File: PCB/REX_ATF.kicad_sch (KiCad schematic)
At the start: 9 parts, among them J1 Tandy_100_102_200_option_rom, J2 JTAG, U1 ATF1504ASL-xAx44, U2 29F800BB

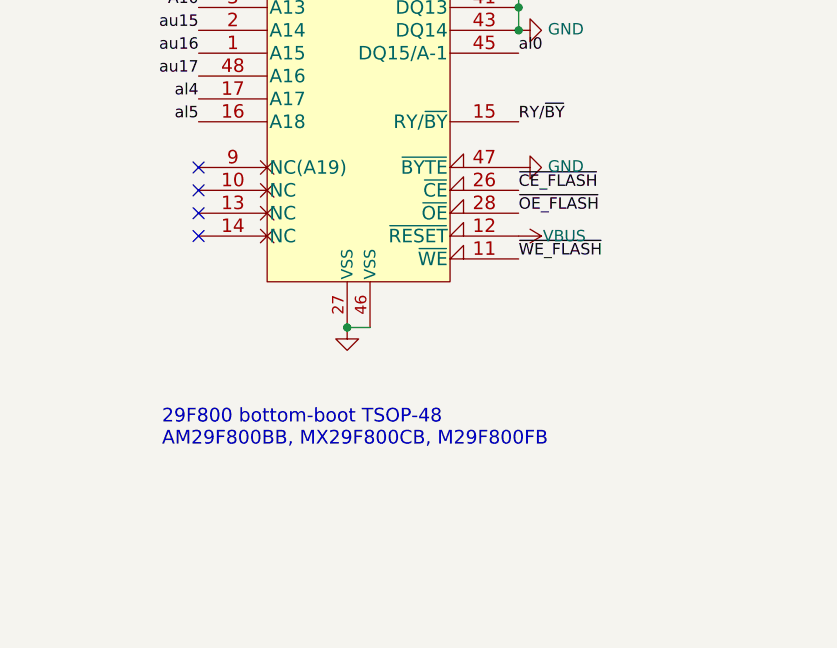
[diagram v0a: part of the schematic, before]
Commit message: use nc pins for pcb ground path
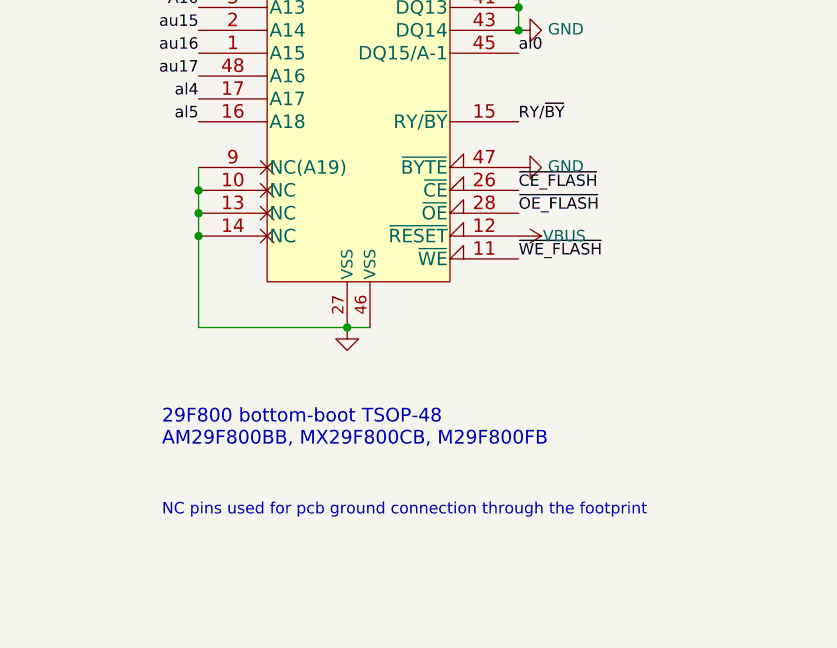
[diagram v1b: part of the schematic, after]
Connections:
- net GND: now also U2.10 (NC), U2.13 (NC), U2.14 (NC), U2.9 (NC(A19))
- no-connect marks 13 -> 9
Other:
- note added: "NC pins used for pcb ground connection through the footprint"
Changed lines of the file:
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@@
 	(title_block
 		(title "REX ATF")
-		(date "2024-07-08")
-		(rev "001")
+		(date "2024-07-22")
+		(rev "002")
 		(company "Brian K. White - b.kenyon.w@gmail.com")
 		(comment 1 "Original design: Steven Adolph")
@@
 	)
 	(junction
+		(at 210.82 104.14)
+		(diameter 0)
+		(color 0 0 0 0)
+	)
+	(junction
 		(at 148.59 113.03)
 		(diameter 0)
@@
 	)
 	(junction
+		(at 210.82 109.22)
+		(diameter 0)
+		(color 0 0 0 0)
+	)
+	(junction
+		(at 210.82 106.68)
+		(diameter 0)
+		(color 0 0 0 0)
+	)
+	(junction
 		(at 146.05 113.03)
 		(diameter 0)
@@
 	)
 	(no_connect
-		(at 210.82 104.14)
-	)
-	(no_connect
-		(at 210.82 109.22)
-	)
-	(no_connect
 		(at 127 69.85)
 	)
@@
 		(at 54.61 67.31)
 	)
-	(no_connect
-		(at 210.82 106.68)
-	)
-	(no_connect
-		(at 210.82 101.6)
-	)
 	(wire
 		(pts
@@
 	(wire
 		(pts
+			(xy 210.82 101.6) (xy 210.82 104.14)
+		)
+		(stroke
+			(width 0)
+			(type default)
+		)
+	)
+	(wire
+		(pts
+			(xy 210.82 109.22) (xy 210.82 119.38)
+		)
+		(stroke
+			(width 0)
+			(type default)
+		)
+	)
+	(wire
+		(pts
 			(xy 246.38 71.12) (xy 246.38 73.66)
 		)
@@
 	(wire
 		(pts
+			(xy 210.82 106.68) (xy 210.82 109.22)
+		)
+		(stroke
+			(width 0)
+			(type default)
+		)
+	)
+	(wire
+		(pts
 			(xy 246.38 73.66) (xy 246.38 76.2)
 		)
@@
 	(wire
 		(pts
+			(xy 210.82 119.38) (xy 227.33 119.38)
+		)
+		(stroke
+			(width 0)
+			(type default)
+		)
+	)
+	(wire
+		(pts
 			(xy 143.51 41.91) (xy 146.05 41.91)
 		)
@@
 	(wire
 		(pts
+			(xy 210.82 104.14) (xy 210.82 106.68)
+		)
+		(stroke
+			(width 0)
+			(type default)
+		)
+	)
+	(wire
+		(pts
 			(xy 148.59 41.91) (xy 151.13 41.91)
 		)
@@
 		)
 	)
+	(text "NC pins used for pcb ground connection through the footprint"
+		(exclude_from_sim no)
+		(at 206.756 139.7 0)
+		(effects
+			(font
+				(size 1.27 1.27)
+			)
+			(justify left)
+		)
+	)

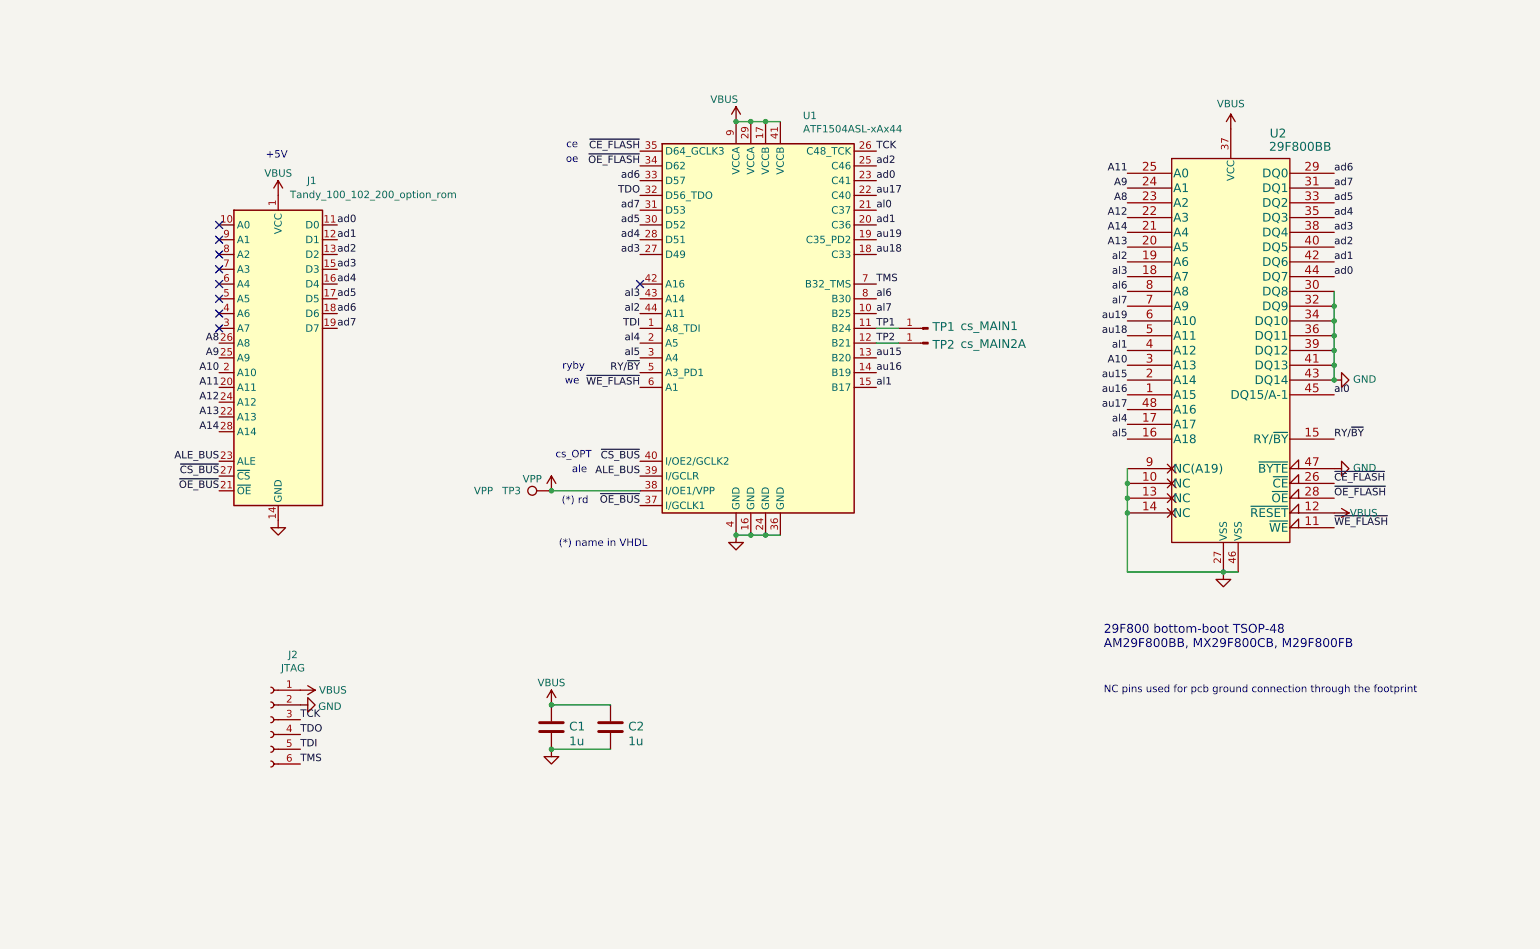
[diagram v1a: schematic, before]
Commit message: move ALE to a GCLK pin and init /CSA & /CSB high
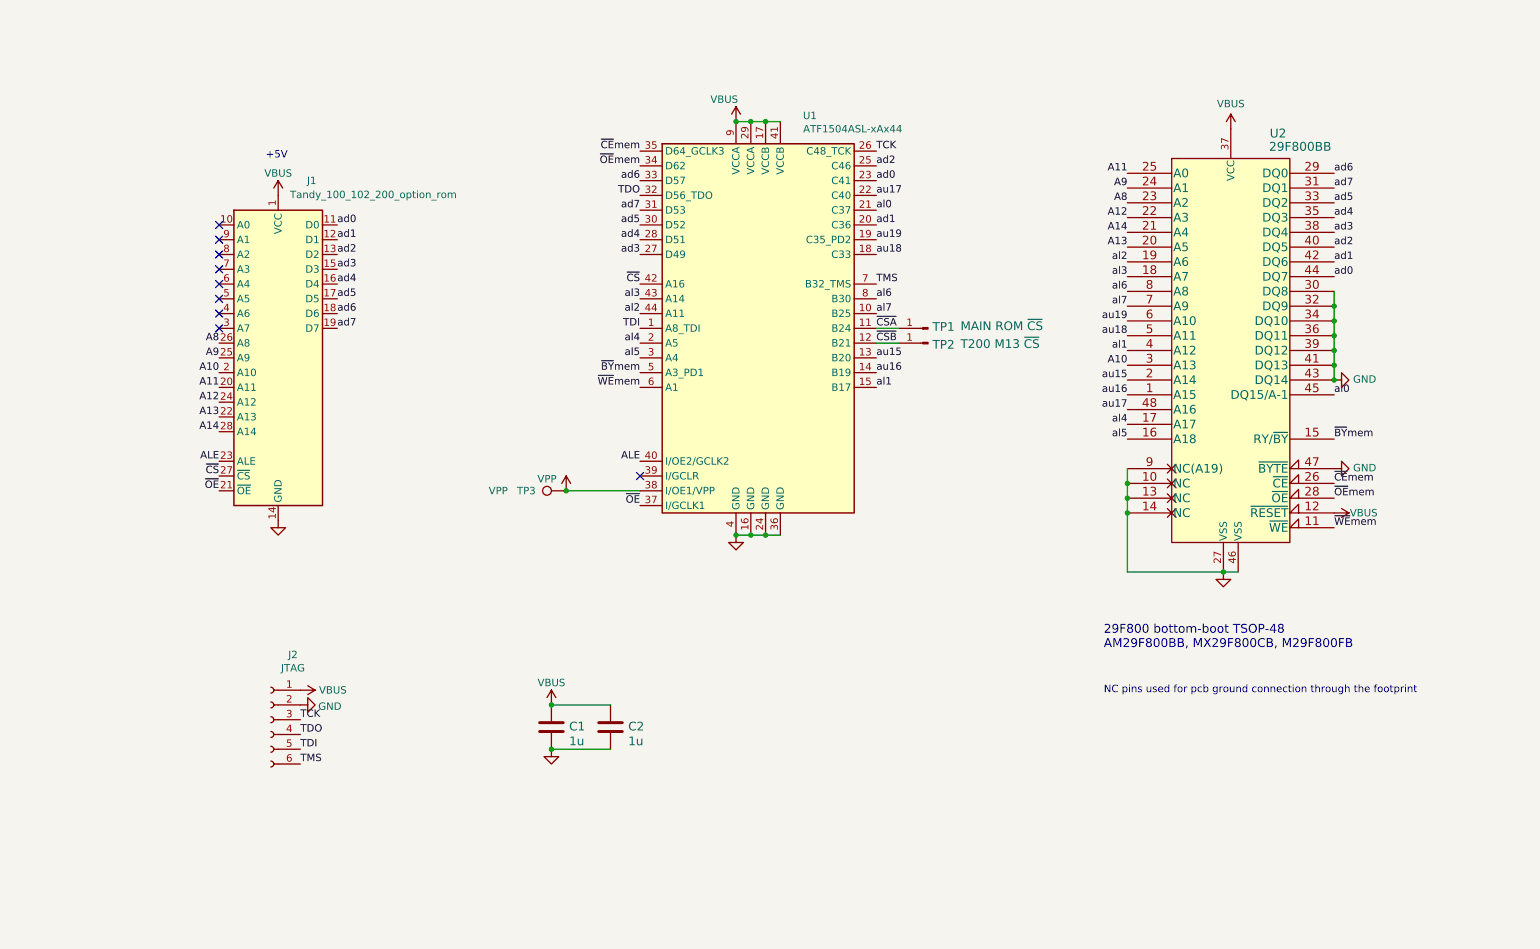
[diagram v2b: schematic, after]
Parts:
- TP1: value cs_MAIN1 -> MAIN ROM ~{CS}
- TP2: value cs_MAIN2A -> T200 M13 ~{CS}
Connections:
- net ~{CS}: now reaches U1.42 (A16)
- net ~{CS}: now also J1.27 (~{CS})
- net ALE_BUS: no longer names the net of U1.39 (I/GCLR)
- net ALE_BUS: no longer J1.23 (ALE)
- net RY/~{BY} renamed ~{BY}mem
- net TP1 renamed ~{CSA}
- net TP2 renamed ~{CSB}
- net ~{CE_FLASH} renamed ~{CE}mem
- net ~{CS_BUS} renamed ALE
- net ALE: now also J1.23 (ALE); no longer J1.27 (~{CS})
- net ~{OE_BUS} renamed ~{OE}
- net ~{OE_FLASH} renamed ~{OE}mem
- net ~{WE_FLASH} renamed ~{WE}mem
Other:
- note removed: "(*) name in VHDL"
- note removed: "(*) rd"
- note removed: "ale"
- note removed: "ce"
- note removed: "cs_OPT"
- note removed: "oe"
- note removed: "ryby"
- note removed: "we"
- moved on the sheet: TP3
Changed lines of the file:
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@@
 	(title_block
 		(title "REX ATF")
-		(date "2024-07-22")
-		(rev "002")
+		(date "2024-07-23")
+		(rev "004")
 		(company "Brian K. White - b.kenyon.w@gmail.com")
 		(comment 1 "Original design: Steven Adolph")
@@
 	)
 	(junction
-		(at 111.76 105.41)
+		(at 114.3 105.41)
 		(diameter 0)
 		(color 0 0 0 0)
@@
 	)
 	(no_connect
-		(at 127 69.85)
+		(at 127 102.87)
 	)
 	(no_connect
@@
 	(wire
 		(pts
-			(xy 111.76 105.41) (xy 127 105.41)
+			(xy 114.3 105.41) (xy 127 105.41)
 		)
 		(stroke
@@
 		)
 	)
-	(text "(*) rd"
-		(exclude_from_sim no)
-		(at 115.824 107.188 0)
-		(effects
-			(font
-				(size 1.27 1.27)
-			)
-		)
-	)
-	(text "ryby"
-		(exclude_from_sim no)
-		(at 115.57 84.074 0)
-		(effects
-			(font
-				(size 1.27 1.27)
-			)
-		)
-	)
-	(text "oe"
-		(exclude_from_sim no)
-		(at 115.316 48.514 0)
-		(effects
-			(font
-				(size 1.27 1.27)
-			)
-		)
-	)
 	(text "29F800 bottom-boot TSOP-48\nAM29F800BB, MX29F800CB, M29F800FB"
 		(exclude_from_sim no)
@@
 		)
 	)
-	(text "ale"
-		(exclude_from_sim no)
-		(at 116.586 101.854 0)
-		(effects
-			(font
-				(size 1.27 1.27)
-			)
-		)
-	)
-	(text "we"
-		(exclude_from_sim no)
-		(at 115.316 86.614 0)
-		(effects
-			(font
-				(size 1.27 1.27)
-			)
-		)
-	)
 	(text "NC pins used for pcb ground connection through the footprint"
 		(exclude_from_sim no)
@@
 		)
 	)
-	(text "(*) name in VHDL"
-		(exclude_from_sim no)
-		(at 113.03 114.554 0)
-		(effects
-			(font
-				(size 1.27 1.27)
-			)
-			(justify left)
-		)
-	)
-	(text "cs_OPT"
-		(exclude_from_sim no)
-		(at 115.57 99.314 0)
-		(effects
-			(font
-				(size 1.27 1.27)
-			)
-		)
-	)
-	(text "ce"
-		(exclude_from_sim no)
-		(at 115.316 45.974 0)
-		(effects
-			(font
-				(size 1.27 1.27)
-			)
-		)
-	)
 	(label "au17"
 		(at 210.82 91.44 180)
@@
 		)
 	)
-	(label "ALE_BUS"
-		(at 127 102.87 180)
-		(fields_autoplaced yes)
-		(effects
-			(font
-				(size 1.27 1.27)
-			)
-			(justify right bottom)
-		)
-	)
-	(label "ALE_BUS"
+	(label "~{BY}mem"
+		(at 246.38 96.52 0)
+		(fields_autoplaced yes)
+		(effects
+			(font
+				(size 1.27 1.27)
+			)
+			(justify left bottom)
+		)
+	)
+	(label "ALE"
+		(at 127 100.33 180)
+		(fields_autoplaced yes)
+		(effects
+			(font
+				(size 1.27 1.27)
+			)
+			(justify right bottom)
+		)
+	)
+	(label "ALE"
 		(at 54.61 100.33 180)
 		(fields_autoplaced yes)
@@
 		)
 	)
-	(label "TP2"
+	(label "~{CSB}"
 		(at 167.64 80.01 0)
 		(fields_autoplaced yes)
@@
 		)
 	)
-	(label "~{WE_FLASH}"
+	(label "~{WE}mem"
 		(at 127 87.63 180)
 		(fields_autoplaced yes)
@@
 		)
 	)
-	(label "TP1"
+	(label "~{CSA}"
 		(at 167.64 77.47 0)
 		(fields_autoplaced yes)
@@
 		)
 	)
-	(label "~{OE_BUS}"
+	(label "~{OE}"
 		(at 127 107.95 180)
 		(fields_autoplaced yes)
@@
 		)
 	)
-	(label "~{OE_FLASH}"
+	(label "~{OE}mem"
 		(at 127 49.53 180)
 		(fields_autoplaced yes)
@@
 		)
 	)
-	(label "RY{slash}~{BY}"
-		(at 246.38 96.52 0)
-		(fields_autoplaced yes)
-		(effects
-			(font
-				(size 1.27 1.27)
-			)
-			(justify left bottom)
-		)
-	)
 	(label "TMS"
 		(at 68.58 152.4 0)
@@
 		)
 	)
-	(label "~{WE_FLASH}"
-		(at 246.38 111.76 0)
-		(fields_autoplaced yes)
-		(effects
-			(font
-				(size 1.27 1.27)
-			)
-			(justify left bottom)
-		)
-	)
 	(label "al5"
 		(at 127 82.55 180)
@@
 		)
 	)
+	(label "~{CE}mem"
+		(at 246.38 104.14 0)
+		(fields_autoplaced yes)
+		(effects
+			(font
+				(size 1.27 1.27)
+			)
+			(justify left bottom)
+		)
+	)
+	(label "~{WE}mem"
+		(at 246.38 111.76 0)
+		(fields_autoplaced yes)
+		(effects
+			(font
+				(size 1.27 1.27)
+			)
+			(justify left bottom)
+		)
+	)
 	(label "A10"
 		(at 54.61 85.09 180)
@@
 		)
 	)
-	(label "~{CS_BUS}"
+	(label "~{CS}"
 		(at 54.61 102.87 180)
 		(fields_autoplaced yes)
@@
 		)
 	)
-	(label "~{CE_FLASH}"
+	(label "~{CE}mem"
 		(at 127 46.99 180)
 		(fields_autoplaced yes)
@@
 		)
 	)
-	(label "RY{slash}~{BY}"
+	(label "~{BY}mem"
 		(at 127 85.09 180)
 		(fields_autoplaced yes)
@@
 		)
 	)
+	(label "~{OE}mem"
+		(at 246.38 106.68 0)
+		(fields_autoplaced yes)
+		(effects
+			(font
+				(size 1.27 1.27)
+			)
+			(justify left bottom)
+		)
+	)
 	(label "ad7"
 		(at 246.38 53.34 0)
@@
 		)
 	)
-	(label "~{CE_FLASH}"
-		(at 246.38 104.14 0)
-		(fields_autoplaced yes)
-		(effects
-			(font
-				(size 1.27 1.27)
-			)
-			(justify left bottom)
-		)
-	)
 	(label "al3"
 		(at 210.82 68.58 180)
@@
 		)
 	)
-	(label "~{CS_BUS}"
-		(at 127 100.33 180)
-		(fields_autoplaced yes)
-		(effects
-			(font
-				(size 1.27 1.27)
-			)
-			(justify right bottom)
-		)
-	)
-	(label "~{OE_BUS}"
+	(label "~{CS}"
+		(at 127 69.85 180)
+		(fields_autoplaced yes)
+		(effects
+			(font
+				(size 1.27 1.27)
+			)
+			(justify right bottom)
+		)
+	)
+	(label "~{OE}"
 		(at 54.61 105.41 180)
 		(fields_autoplaced yes)
@@
 			)
 			(justify right bottom)
-		)
-	)
-	(label "~{OE_FLASH}"
-		(at 246.38 106.68 0)
-		(fields_autoplaced yes)
-		(effects
-			(font
-				(size 1.27 1.27)
-			)
-			(justify left bottom)
 		)
 	)
@@
 			)
 		)
-		(property "Value" "cs_MAIN1"
+		(property "Value" "MAIN ROM ~{CS}"
 			(at 182.118 76.2 0)
 			(effects
@@
 			)
 		)
-		(property "Value" "cs_MAIN2A"
+		(property "Value" "T200 M13 ~{CS}"
 			(at 182.118 81.026 0)
 			(effects
@@
 	(symbol
 		(lib_id "000_LOCAL:TestPoint")
-		(at 111.76 105.41 90)
+		(at 114.3 105.41 90)
 		(unit 1)
 		(exclude_from_sim no)
@@
 		(dnp no)
 		(property "Reference" "TP3"
-			(at 104.902 105.41 90)
+			(at 107.442 105.41 90)
 			(effects
 				(font
@@
 		)
 		(property "Value" "VPP"
-			(at 100.076 105.41 90)
+			(at 102.616 105.41 90)
 			(effects
 				(font
@@
 		)
 		(property "Footprint" "000_LOCAL:TP_D0.8"
-			(at 111.76 100.33 0)
+			(at 114.3 100.33 0)
 			(effects
 				(font
@@
 		)
 		(property "Datasheet" "~"
-			(at 111.76 100.33 0)
+			(at 114.3 100.33 0)
 			(effects
 				(font
@@
 		)
 		(property "Description" "test point"
-			(at 111.76 105.41 0)
+			(at 114.3 105.41 0)
 			(effects
 				(font
@@
 	(symbol
 		(lib_id "power:VPP")
-		(at 111.76 105.41 0)
+		(at 114.3 105.41 0)
 		(unit 1)
 		(exclude_from_sim no)
@@
 		(dnp no)
 		(property "Reference" "#PWR08"
-			(at 111.76 109.22 0)
+			(at 114.3 109.22 0)
 			(effects
 				(font
@@
 		)
 		(property "Value" "VPP"
-			(at 108.458 103.378 0)
+			(at 110.998 103.378 0)
 			(effects
 				(font
@@
 		)
 		(property "Footprint" ""
-			(at 111.76 105.41 0)
+			(at 114.3 105.41 0)
 			(effects
 				(font
@@
 		)
 		(property "Datasheet" ""
-			(at 111.76 105.41 0)
+			(at 114.3 105.41 0)
 			(effects
 				(font
@@
 		)
 		(property "Description" "Power symbol creates a global label with name \"VPP\""
-			(at 111.76 105.41 0)
-			(effects
-				(font
+			(at 114.3 105.41 0)
+			(effects
+				(font
